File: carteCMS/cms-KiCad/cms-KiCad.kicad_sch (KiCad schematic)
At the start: 6 parts, among them J1 Conn_01x02, SW1 SW_SPDT

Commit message: v2 - schéma et empruntes terminés (normalement)
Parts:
- J1: footprint (none) -> accordeurEmp:conn01x02Alim-CTB52022
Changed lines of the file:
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@@
+	(wire
+		(pts
+			(xy 31.75 147.32) (xy 34.29 147.32)
+		)
+		(stroke
+			(width 0)
+			(type default)
+		)
+	)
 	(wire
 		(pts
 			(xy 36.83 147.32) (xy 43.18 147.32)
-		)
-		(stroke
-			(width 0)
-			(type default)
-		)
-	)
-	(wire
-		(pts
-			(xy 34.29 147.32) (xy 31.75 147.32)
 		)
 		(stroke
@@
 			)
 		)
-		(property "Footprint" ""
+		(property "Footprint" "accordeurEmp:conn01x02Alim-CTB52022"
 			(at 34.29 142.24 0)
 			(effects
@@
 		)
 		(instances
-			(project "projet-KiCad"
+			(project "cms-KiCad"
 				(path "/59f7da0b-cec5-4ac9-8c02-026d0daeaa65"
 					(page "2")
@@
 		)
 		(instances
-			(project "projet-KiCad"
+			(project "cms-KiCad"
 				(path "/59f7da0b-cec5-4ac9-8c02-026d0daeaa65"
 					(page "3")

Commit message: Début routage (avant pistes)
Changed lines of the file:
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@@
 	(wire
 		(pts
-			(xy 184.15 68.58) (xy 184.15 41.91)
+			(xy 166.37 113.03) (xy 166.37 86.36)
 		)
 		(stroke
@@
 	(wire
 		(pts
-			(xy 144.78 69.85) (xy 144.78 41.91)
-		)
-		(stroke
-			(width 0)
-			(type default)
-		)
-	)
-	(wire
-		(pts
-			(xy 177.8 68.58) (xy 184.15 68.58)
+			(xy 127 114.3) (xy 127 86.36)
+		)
+		(stroke
+			(width 0)
+			(type default)
+		)
+	)
+	(wire
+		(pts
+			(xy 160.02 113.03) (xy 166.37 113.03)
 		)
 		(stroke
@@
 	(wire
 		(pts
-			(xy 152.4 69.85) (xy 144.78 69.85)
+			(xy 134.62 114.3) (xy 127 114.3)
 		)
 		(stroke
@@
 	(wire
 		(pts
-			(xy 184.15 41.91) (xy 177.8 41.91)
+			(xy 166.37 86.36) (xy 160.02 86.36)
 		)
 		(stroke
@@
 	(wire
 		(pts
-			(xy 144.78 41.91) (xy 152.4 41.91)
+			(xy 127 86.36) (xy 134.62 86.36)
 		)
 		(stroke
@@
 		)
 		(instances
-			(project "projet-KiCad"
+			(project "cms-KiCad"
 				(path "/59f7da0b-cec5-4ac9-8c02-026d0daeaa65"
 					(reference "C1")
@@
 		)
 		(instances
-			(project "projet-KiCad"
+			(project "cms-KiCad"
 				(path "/59f7da0b-cec5-4ac9-8c02-026d0daeaa65"
 					(reference "#FLG02")
@@
 		)
 		(instances
-			(project "projet-KiCad"
+			(project "cms-KiCad"
 				(path "/59f7da0b-cec5-4ac9-8c02-026d0daeaa65"
 					(reference "R1")
@@
 		)
 		(instances
-			(project "projet-KiCad"
+			(project "cms-KiCad"
 				(path "/59f7da0b-cec5-4ac9-8c02-026d0daeaa65"
 					(reference "#PWR02")
@@
 		)
 		(instances
-			(project "projet-KiCad"
+			(project "cms-KiCad"
 				(path "/59f7da0b-cec5-4ac9-8c02-026d0daeaa65"
 					(reference "D2")
@@
 		)
 		(instances
-			(project "projet-KiCad"
+			(project "cms-KiCad"
 				(path "/59f7da0b-cec5-4ac9-8c02-026d0daeaa65"
 					(reference "SW1")
@@
 		)
 		(instances
-			(project "projet-KiCad"
+			(project "cms-KiCad"
 				(path "/59f7da0b-cec5-4ac9-8c02-026d0daeaa65"
 					(reference "#FLG03")
@@
 		)
 		(instances
-			(project "projet-KiCad"
+			(project "cms-KiCad"
 				(path "/59f7da0b-cec5-4ac9-8c02-026d0daeaa65"
 					(reference "J1")
@@
 		)
 		(instances
-			(project "projet-KiCad"
+			(project "cms-KiCad"
 				(path "/59f7da0b-cec5-4ac9-8c02-026d0daeaa65"
 					(reference "D1")
@@
 		)
 		(instances
-			(project "projet-KiCad"
+			(project "cms-KiCad"
 				(path "/59f7da0b-cec5-4ac9-8c02-026d0daeaa65"
 					(reference "#PWR01")
@@
 	)
 	(sheet
-		(at 152.4 38.1)
+		(at 134.62 82.55)
 		(size 25.4 12.7)
 		(fields_autoplaced yes)
@@
 		)
 		(property "Sheetname" "Analog"
-			(at 152.4 37.3884 0)
+			(at 134.62 81.8384 0)
 			(effects
 				(font
@@
 		)
 		(property "Sheetfile" "accordeur_analog.kicad_sch"
-			(at 152.4 51.3846 0)
+			(at 134.62 95.8346 0)
 			(effects
 				(font
@@
 		)
 		(pin "Fmesure" output
-			(at 177.8 41.91 0)
+			(at 160.02 86.36 0)
 			(effects
 				(font
@@
 		)
 		(pin "100xFc" input
-			(at 152.4 41.91 180)
+			(at 134.62 86.36 180)
 			(effects
 				(font
@@
 	)
 	(sheet
-		(at 152.4 63.5)
+		(at 134.62 107.95)
 		(size 25.4 12.7)
 		(fields_autoplaced yes)
@@
 		)
 		(property "Sheetname" "Num"
-			(at 152.4 62.7884 0)
+			(at 134.62 107.2384 0)
 			(effects
 				(font
@@
 		)
 		(property "Sheetfile" "accordeur_num.kicad_sch"
-			(at 152.4 76.7846 0)
+			(at 134.62 121.2346 0)
 			(effects
 				(font
@@
 		)
 		(pin "Fmesure" input
-			(at 177.8 68.58 0)
+			(at 160.02 113.03 0)
 			(effects
 				(font
@@
 		)
 		(pin "100xFc" output
-			(at 152.4 69.85 180)
-			(effects
-				(font
+			(at 134.62 114.3 180)
+			(effects
+				(font

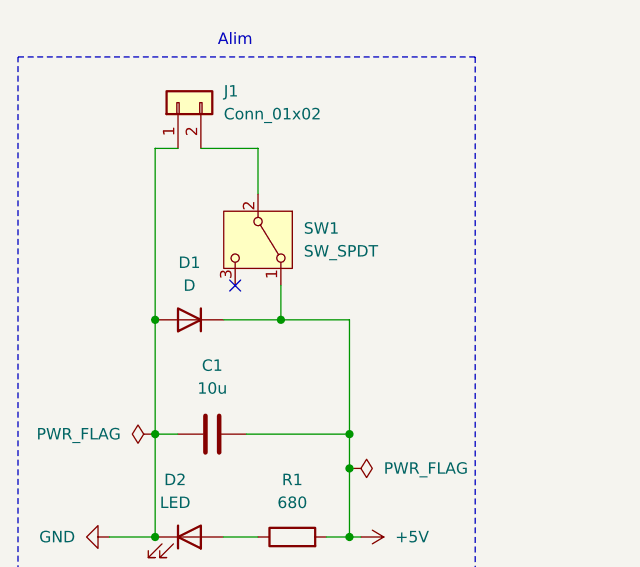
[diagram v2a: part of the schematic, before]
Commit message: projet final
schéma, routage, librairies et fichiers de fabrication
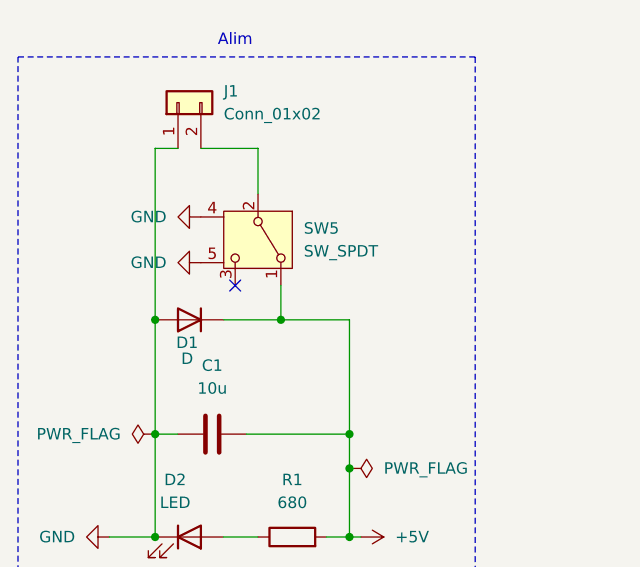
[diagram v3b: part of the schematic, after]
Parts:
- removed SW1: SW_SPDT, accordeurEmp:SWITCH_11MA1QS1, symbol Switch:SW_SPDT
- added SW5: SW_SPDT, accordeurEmp:SWITCH_11MA1QS1, symbol accordeurSym:SW_SPDT
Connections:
- net +5V: now also SW5.1 (A)
- net GND: now also SW5.4 (carcasse1), SW5.5 (carcasse2)
- net at J1.2 (Pin_2): now also SW5.2 (B)
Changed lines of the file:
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@@
+	)
+	(symbol
+		(lib_id "power:GND")
+		(at 36.83 154.94 270)
+		(unit 1)
+		(exclude_from_sim no)
+		(in_bom yes)
+		(on_board yes)
+		(dnp no)
+		(fields_autoplaced yes)
+		(property "Reference" "#PWR034"
+			(at 30.48 154.94 0)
+			(effects
+				(font
+					(size 1.27 1.27)
+				)
+				(hide yes)
+			)
+		)
+		(property "Value" "GND"
+			(at 33.02 154.9399 90)
+			(effects
+				(font
+					(size 1.27 1.27)
+				)
+				(justify right)
+			)
+		)
+		(property "Footprint" ""
+			(at 36.83 154.94 0)
+			(effects
+				(font
+					(size 1.27 1.27)
+				)
+				(hide yes)
+			)
+		)
+		(property "Datasheet" ""
+			(at 36.83 154.94 0)
+			(effects
+				(font
+					(size 1.27 1.27)
+				)
+				(hide yes)
+			)
+		)
+		(property "Description" "Power symbol creates a global label with name \"GND\" , ground"
+			(at 36.83 154.94 0)
+			(effects
+				(font
+					(size 1.27 1.27)
+				)
+				(hide yes)
+			)
+		)
+		(pin "1"
+		)
+		(instances
+			(project "cms-KiCad"
+				(path "/59f7da0b-cec5-4ac9-8c02-026d0daeaa65"
+					(reference "#PWR034")
+					(unit 1)
+				)
+			)
+		)
 	)
 	(symbol
@@
 	)
 	(symbol
+		(lib_id "accordeurSym:SW_SPDT")
+		(at 43.18 157.48 270)
+		(unit 1)
+		(exclude_from_sim no)
+		(in_bom yes)
+		(on_board yes)
+		(dnp no)
+		(fields_autoplaced yes)
+		(property "Reference" "SW5"
+			(at 48.26 156.2099 90)
+			(effects
+				(font
+					(size 1.27 1.27)
+				)
+				(justify left)
+			)
+		)
+		(property "Value" "SW_SPDT"
+			(at 48.26 158.7499 90)
+			(effects
+				(font
+					(size 1.27 1.27)
+				)
+				(justify left)
+			)
+		)
+		(property "Footprint" "accordeurEmp:SWITCH_11MA1QS1"
+			(at 48.26 157.48 0)
+			(effects
+				(font
+					(size 1.27 1.27)
+				)
+				(hide yes)
+			)
+		)
+		(property "Datasheet" "~"
+			(at 35.56 157.48 0)
+			(effects
+				(font
+					(size 1.27 1.27)
+				)
+				(hide yes)
+			)
+		)
+		(property "Description" "Switch, single pole double throw"
+			(at 43.18 157.48 0)
+			(effects
+				(font
+					(size 1.27 1.27)
+				)
+				(hide yes)
+			)
+		)
+		(pin "4"
+		)
+		(pin "1"
+		)
+		(pin "5"
+		)
+		(pin "2"
+		)
+		(pin "3"
+		)
+		(instances
+			(project "cms-KiCad"
+				(path "/59f7da0b-cec5-4ac9-8c02-026d0daeaa65"
+					(reference "SW5")
+					(unit 1)
+				)
+			)
+		)
+	)
+	(symbol
 		(lib_id "Device:LED")
 		(at 35.56 190.5 0)
@@
 	)
 	(symbol
-		(lib_id "Switch:SW_SPDT")
-		(at 43.18 157.48 270)
-		(unit 1)
-		(exclude_from_sim no)
-		(in_bom yes)
-		(on_board yes)
-		(dnp no)
-		(fields_autoplaced yes)
-		(property "Reference" "SW1"
-			(at 48.26 156.2099 90)
-			(effects
-				(font
-					(size 1.27 1.27)
-				)
-				(justify left)
-			)
-		)
-		(property "Value" "SW_SPDT"
-			(at 48.26 158.7499 90)
-			(effects
-				(font
-					(size 1.27 1.27)
-				)
-				(justify left)
-			)
-		)
-		(property "Footprint" "accordeurEmp:SWITCH_11MA1QS1"
-			(at 43.18 157.48 0)
-			(effects
-				(font
-					(size 1.27 1.27)
-				)
-				(hide yes)
-			)
-		)
-		(property "Datasheet" "~"
-			(at 35.56 157.48 0)
-			(effects
-				(font
-					(size 1.27 1.27)
-				)
-				(hide yes)
-			)
-		)
-		(property "Description" "Switch, single pole double throw"
-			(at 43.18 157.48 0)
-			(effects
-				(font
-					(size 1.27 1.27)
-				)
-				(hide yes)
-			)
-		)
-		(pin "2"
-		)
-		(pin "3"
-		)
-		(pin "1"
-		)
-		(instances
-			(project "cms-KiCad"
-				(path "/59f7da0b-cec5-4ac9-8c02-026d0daeaa65"
-					(reference "SW1")
-					(unit 1)
-				)
-			)
-		)
-	)
-	(symbol
 		(lib_id "power:PWR_FLAG")
 		(at 53.34 182.88 270)
@@
 	)
 	(symbol
+		(lib_id "power:GND")
+		(at 36.83 160.02 270)
+		(unit 1)
+		(exclude_from_sim no)
+		(in_bom yes)
+		(on_board yes)
+		(dnp no)
+		(fields_autoplaced yes)
+		(property "Reference" "#PWR035"
+			(at 30.48 160.02 0)
+			(effects
+				(font
+					(size 1.27 1.27)
+				)
+				(hide yes)
+			)
+		)
+		(property "Value" "GND"
+			(at 33.02 160.0199 90)
+			(effects
+				(font
+					(size 1.27 1.27)
+				)
+				(justify right)
+			)
+		)
+		(property "Footprint" ""
+			(at 36.83 160.02 0)
+			(effects
+				(font
+					(size 1.27 1.27)
+				)
+				(hide yes)
+			)
+		)
+		(property "Datasheet" ""
+			(at 36.83 160.02 0)
+			(effects
+				(font
+					(size 1.27 1.27)
+				)
+				(hide yes)
+			)
+		)
+		(property "Description" "Power symbol creates a global label with name \"GND\" , ground"
+			(at 36.83 160.02 0)
+			(effects
+				(font
+					(size 1.27 1.27)
+				)
+				(hide yes)
+			)
+		)
+		(pin "1"
+		)
+		(instances
+			(project "cms-KiCad"
+				(path "/59f7da0b-cec5-4ac9-8c02-026d0daeaa65"
+					(reference "#PWR035")
+					(unit 1)
+				)
+			)
+		)
+	)
+	(symbol
 		(lib_id "Connector_Generic:Conn_01x02")
 		(at 34.29 142.24 90)
@@
 		(on_board yes)
 		(dnp no)
-		(fields_autoplaced yes)
 		(property "Reference" "D1"
-			(at 35.56 160.02 0)
+			(at 35.306 168.91 0)
 			(effects
 				(font
@@
 		)
 		(property "Value" "D"
-			(at 35.56 162.56 0)
-			(effects
-				(font
+			(at 35.306 170.688 0)
+			(effects
+				(font
